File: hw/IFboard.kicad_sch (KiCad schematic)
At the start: 79 parts, among them J1 USB_C_Receptacle_USB2.0_16P, J2 Conn_01x03_Socket, J3 Conn_ARM_SWD_TagConnect_TC203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, J4 Conn_01x03_Socket, J5 Conn_01x03_Socket, J6 Conn_01x03_Socket, J7 Conn_01x01_MountingPin, SW3 SW_Push, SW4 SW_Push, SW5 SW_Push, SW6 SW_Push, U1 AMS1117-3.3, U2 XC6206PxxxMR, U3 TCAN3413DR, U4 ST4E1240DT, U5 MAX232ESE+T, U6 STM32G0B1CBTx, U7 ER_OLEDM0.91_1x-I2C

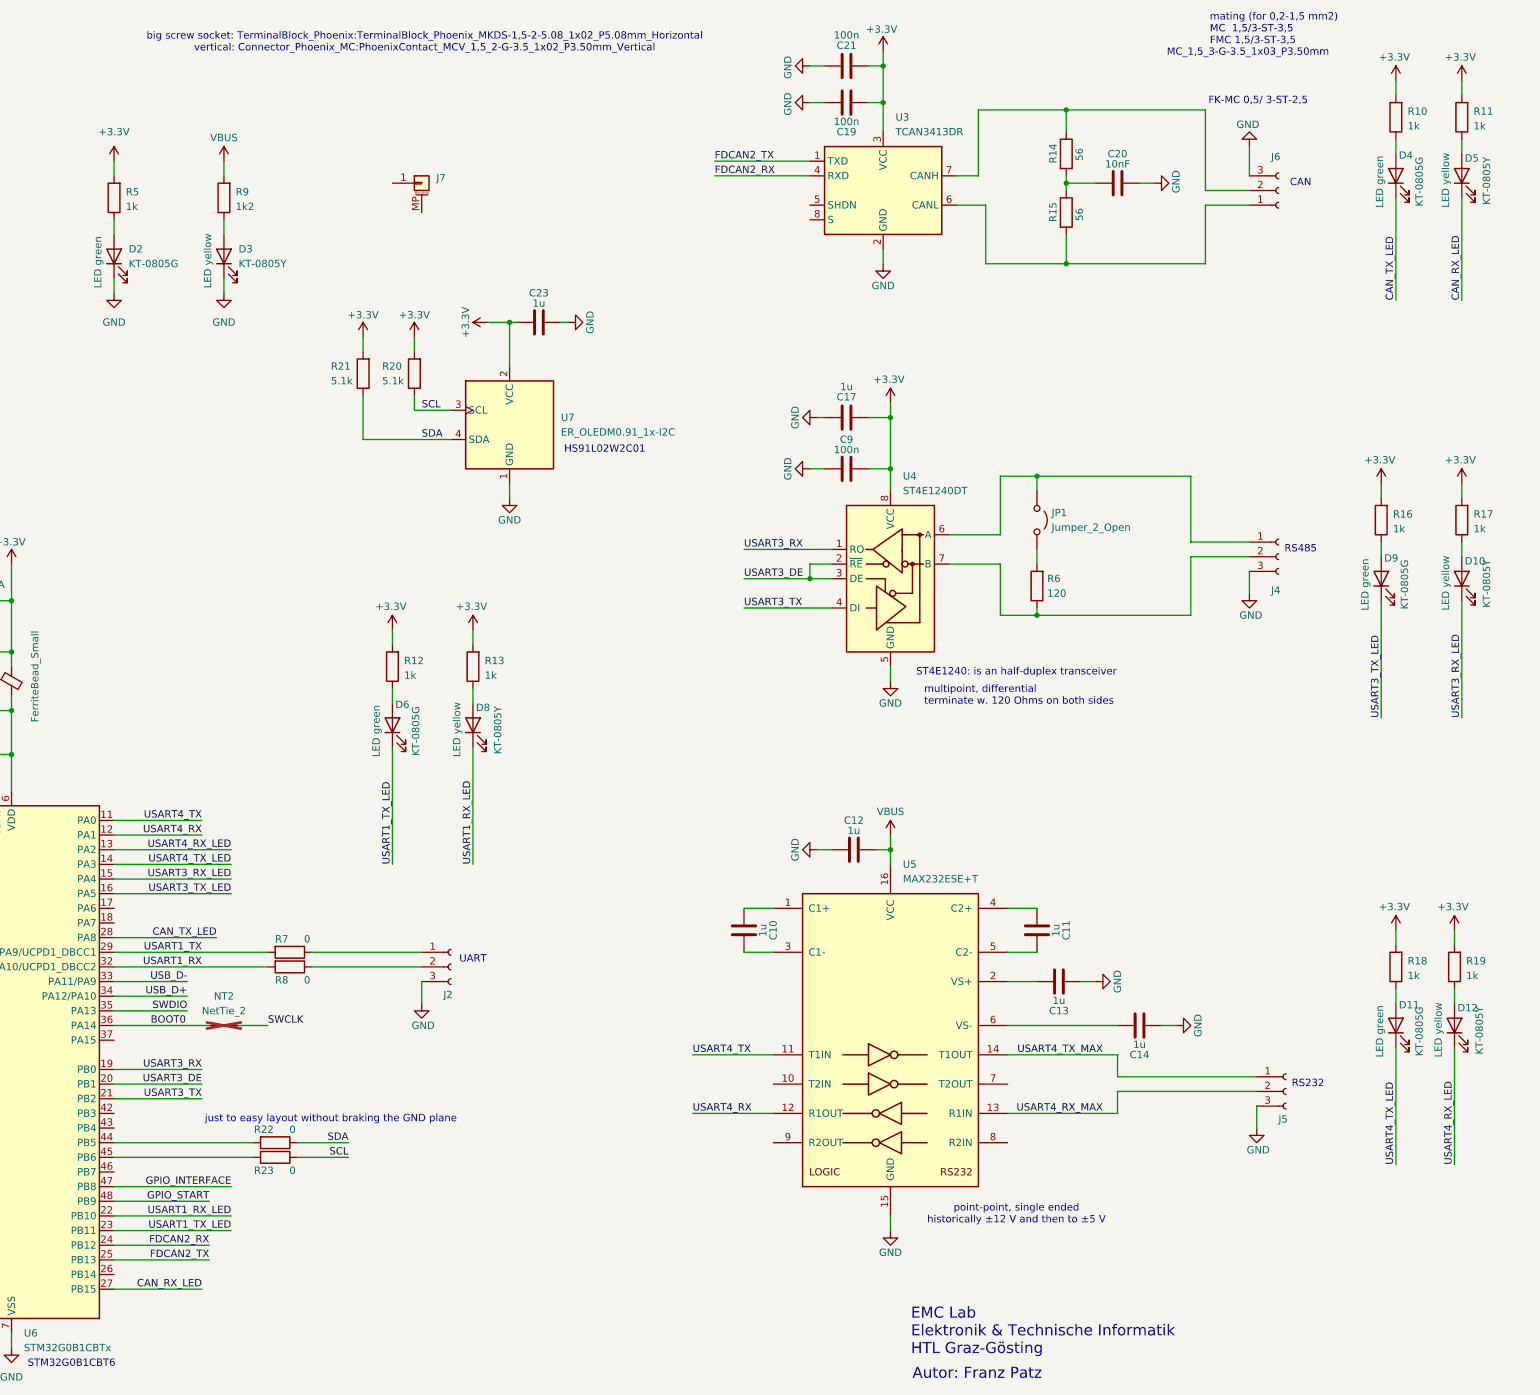
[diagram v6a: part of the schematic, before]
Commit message: swapped poition of two connectors for better routing
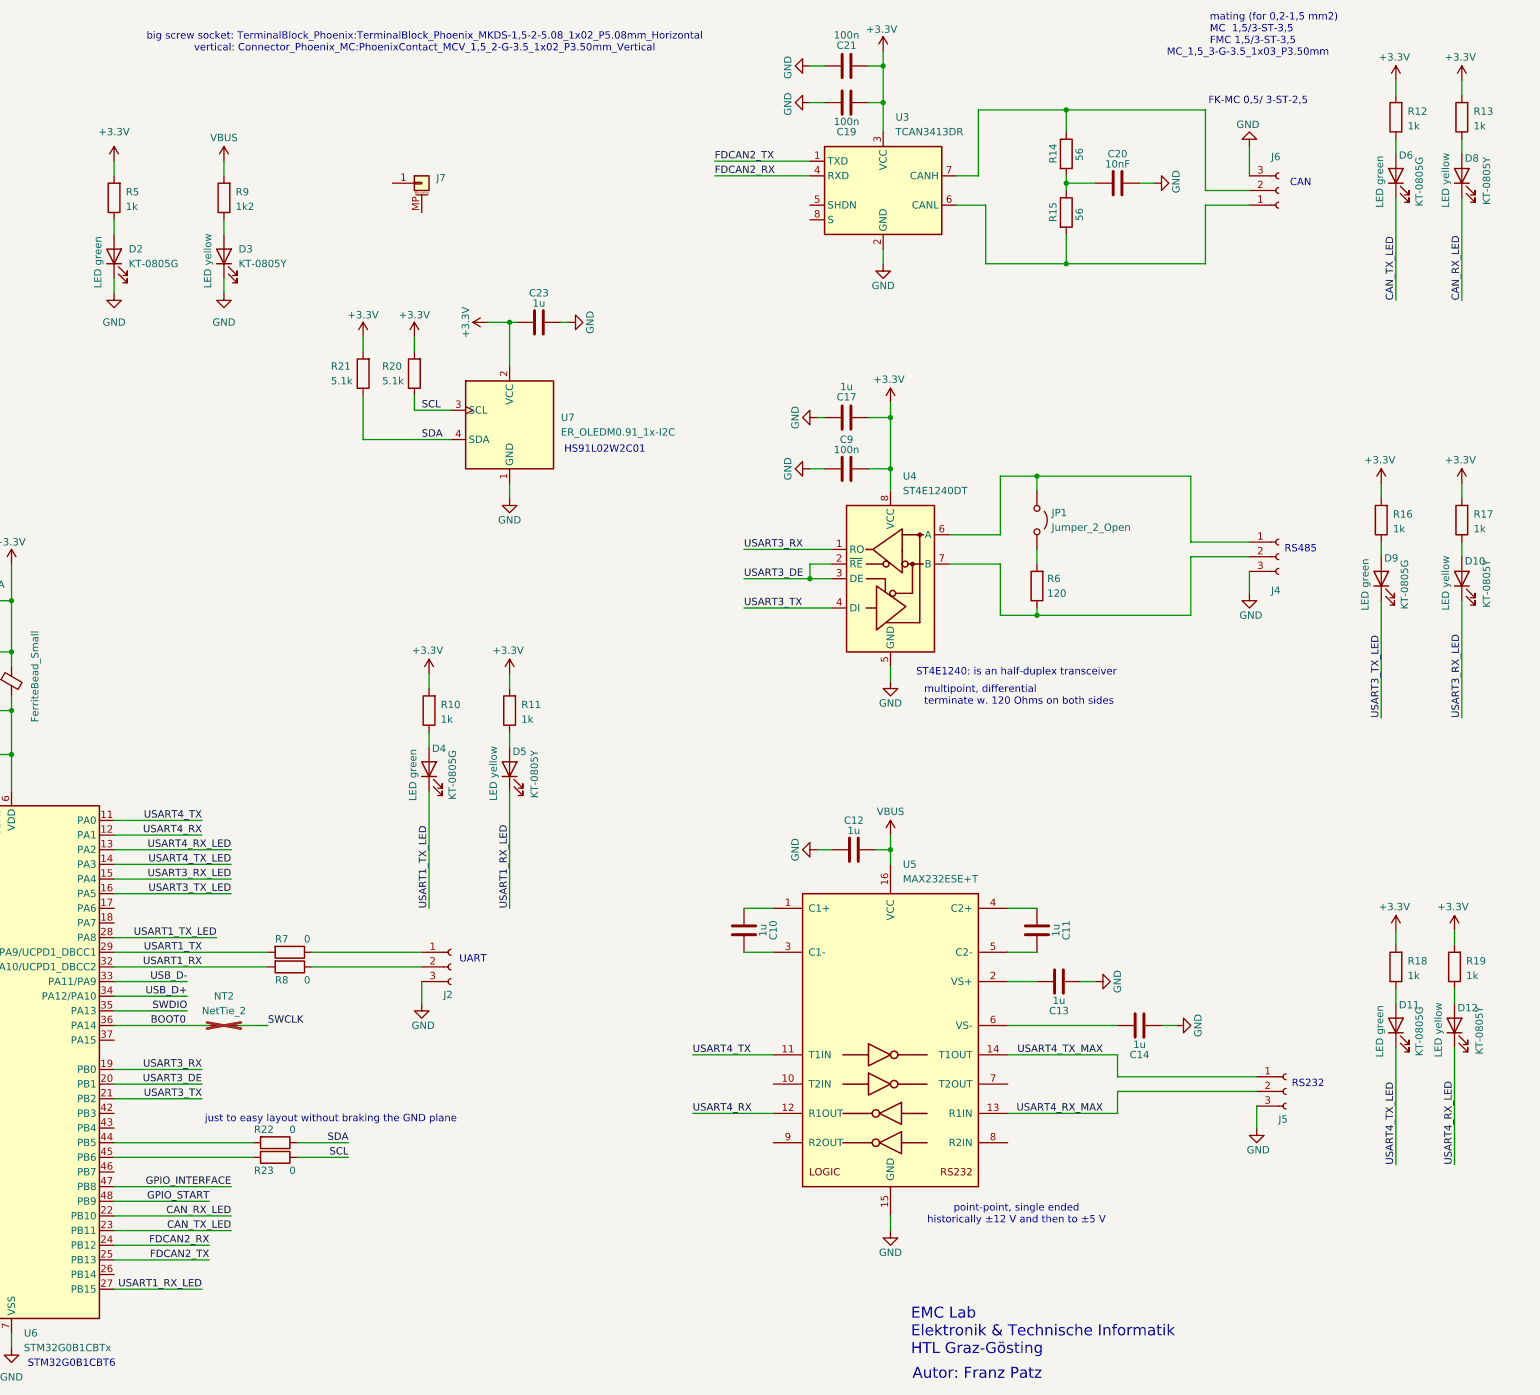
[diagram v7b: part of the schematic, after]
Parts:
- J6: footprint Connector_Phoenix_MC:PhoenixContact_MC_1,5_3-G-3.5_1x03_P3.50mm_Horizontal -> PZL:1881451
- renumbered D6 to D4, D8 to D5, D4 to D6, D5 to D8, R12 to R10, R13 to R11, R10 to R12, R11 to R13
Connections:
- net CAN_RX_LED: now also U6.22 (PB10); no longer U6.27 (PB15)
- net CAN_TX_LED: now also U6.23 (PB11); no longer U6.28 (PA8)
- net USART1_RX_LED: now also U6.27 (PB15); no longer U6.22 (PB10)
- net USART1_TX_LED: now also U6.28 (PA8); no longer U6.23 (PB11)
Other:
- moved on the sheet: D4, D5, R10, R11

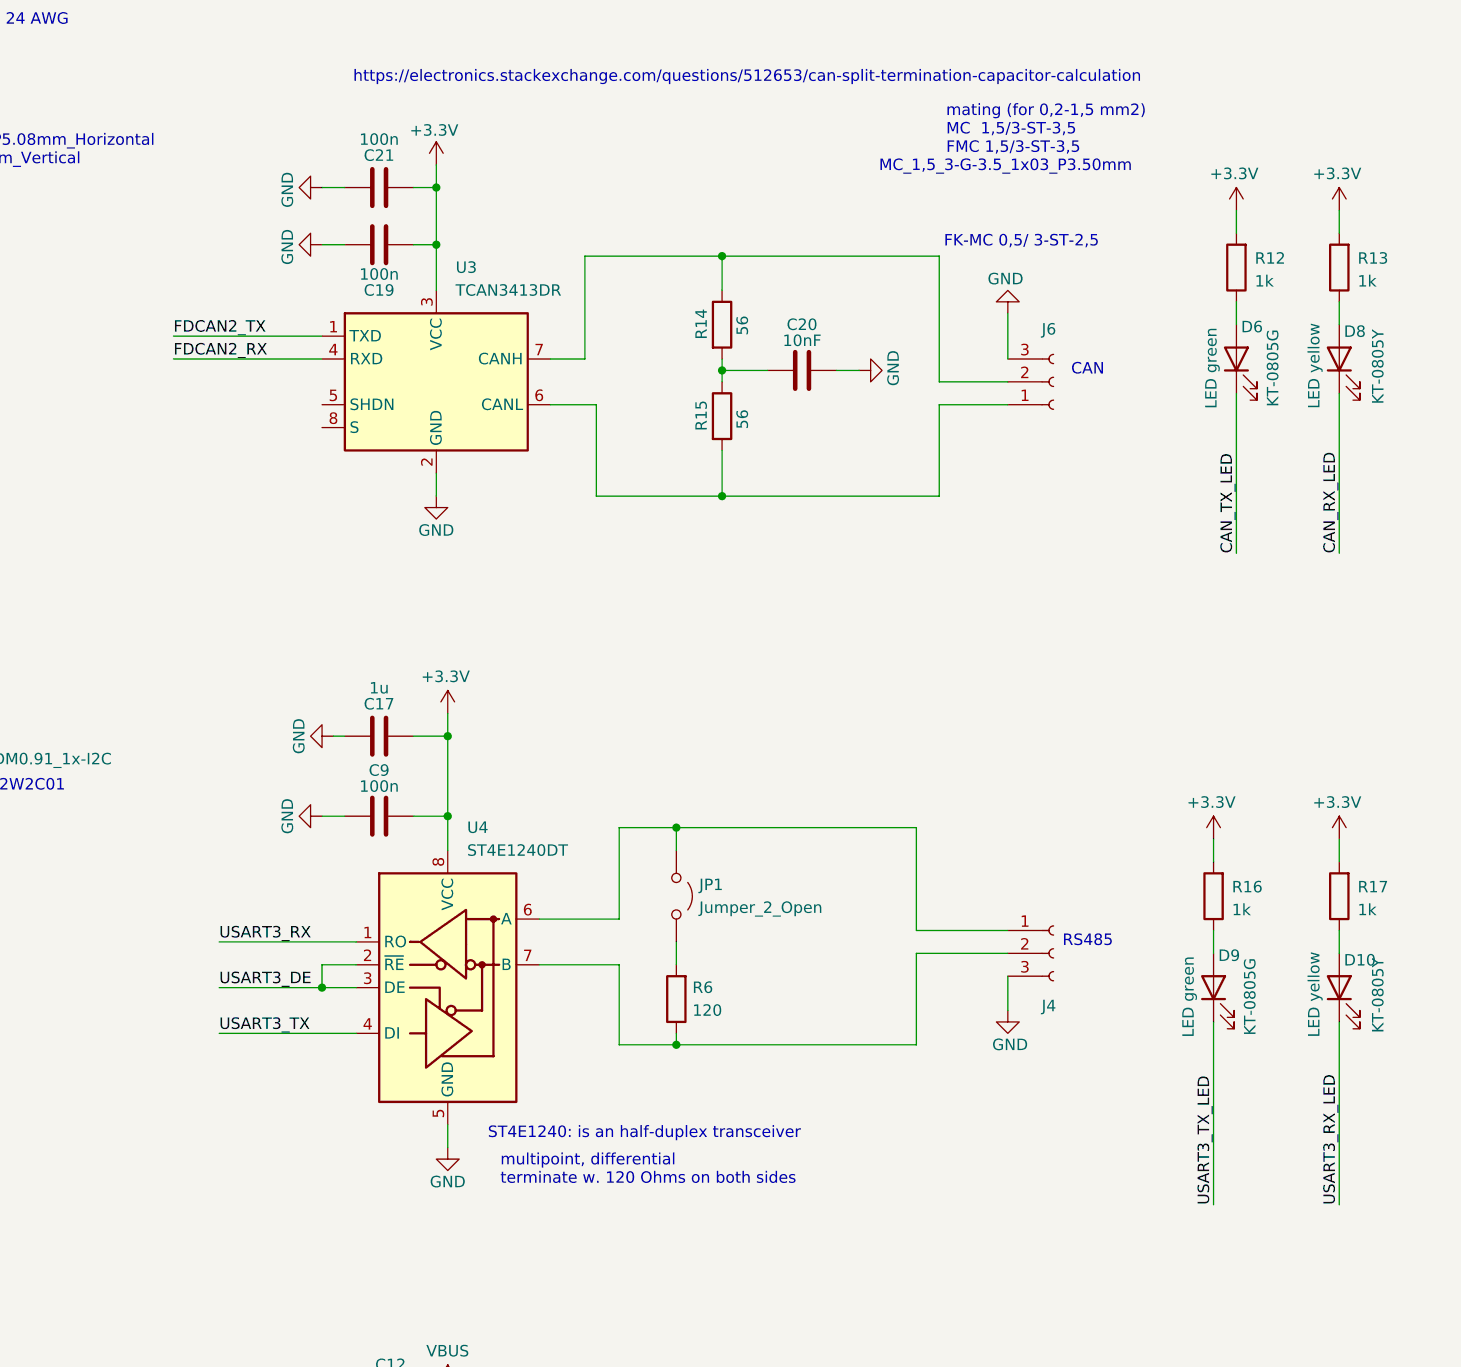
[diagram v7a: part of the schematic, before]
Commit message: added CMCs to RS485 and CAN interfaces
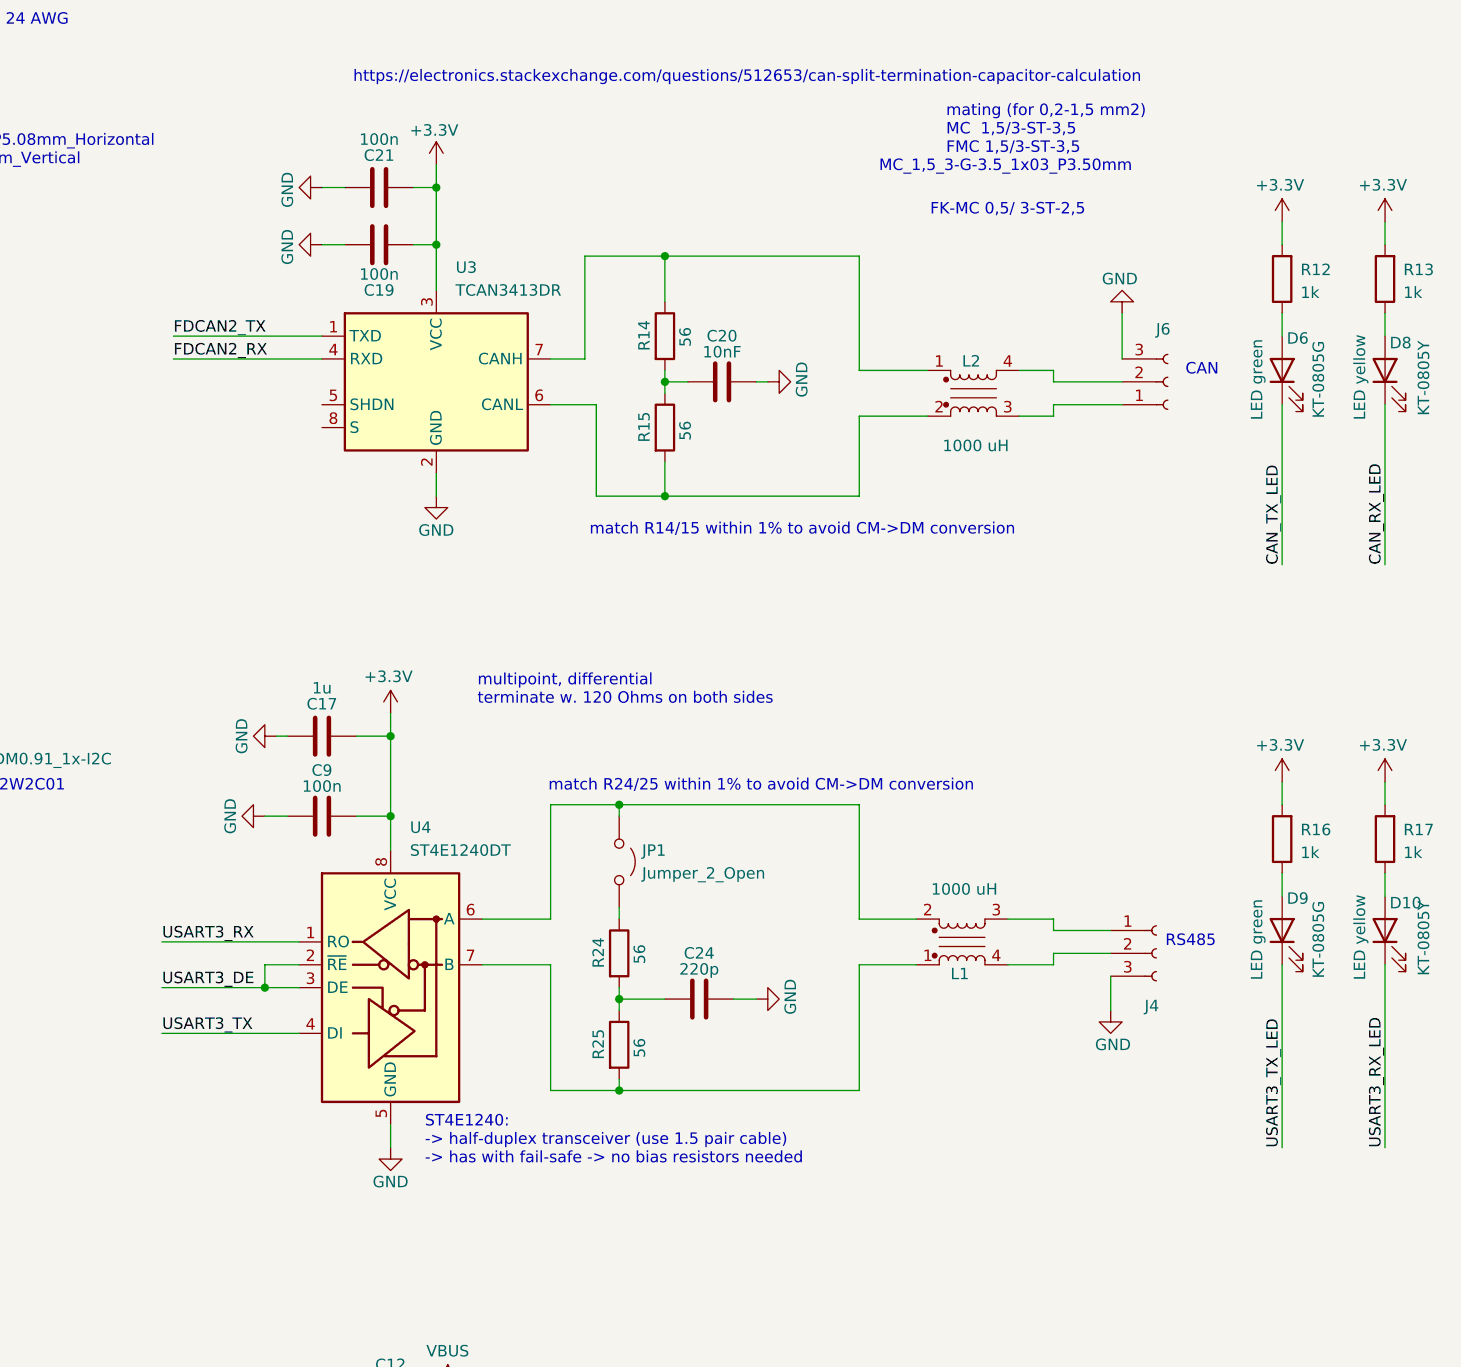
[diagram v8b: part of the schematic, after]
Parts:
- removed R6: 120, Resistor_SMD:R_1206_3216Metric, symbol Device:R
- added C24: 220p, Capacitor_SMD:C_0402_1005Metric, symbol Device:C
- added L1, L2: 1000 uH, PZL:L_Wurth_WE-SL2-74422x, symbol newLib:74422x_744222
- added R24, R25: 56, Resistor_SMD:R_0805_2012Metric, symbol Device:R
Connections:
- net GND: now also C24.1
- net at JP1.1 (A), U4.6 (A): now also L1.2; no longer J4.1 (Pin_1)
- net at U4.7 (B): now also L1.1, R25.2; no longer J4.2 (Pin_2)
- net at R15.2, U3.6 (CANL): now also L2.2; no longer J6.1 (Pin_1)
- net at R14.1, U3.7 (CANH): now also L2.1; no longer J6.2 (Pin_2)
- net at JP1.2 (B): now also R24.1
- new net: C24.2, R24.2, R25.1
- new net: J4.1 (Pin_1), L1.3
- new net: J4.2 (Pin_2), L1.4
- new net: J6.1 (Pin_1), L2.3
- new net: J6.2 (Pin_2), L2.4
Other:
- note added: "ST4E1240: -> half-duplex transceiver (use 1.5 pair cable) -> has with fail-safe -> no bias resistors needed"
- note added: "match R14/15 within 1% to avoid CM->DM conversion"
- note added: "match R24/25 within 1% to avoid CM->DM conversion"
- note removed: "ST4E1240: is an half-duplex transceiver"
- moved on the sheet: C17, C20, C9, D10, D6, D8, D9, J4, J6, JP1, R12, R13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
